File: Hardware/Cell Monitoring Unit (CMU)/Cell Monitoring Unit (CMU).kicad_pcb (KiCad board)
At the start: 4 copper layers, 144.7 x 95.9 mm, 171 parts, among them J1 TEST, J10 NTC-5, J11 NTC-6, J12 NTC-7, J13 NTC-8, J2 LOW SIDE, J3 12S, J4 705550056, J5 HIGH SIDE, J6 NTC-1, J7 NTC-2, J8 NTC-3, J9 NTC-4, T1 CEP99-102, T2 CEP99-102, U1 PESD5V0L2BT, U2 PESD5V0L2BT, U3 ZXTN4004KQTC, U4 PBQ79616PAPTQ1

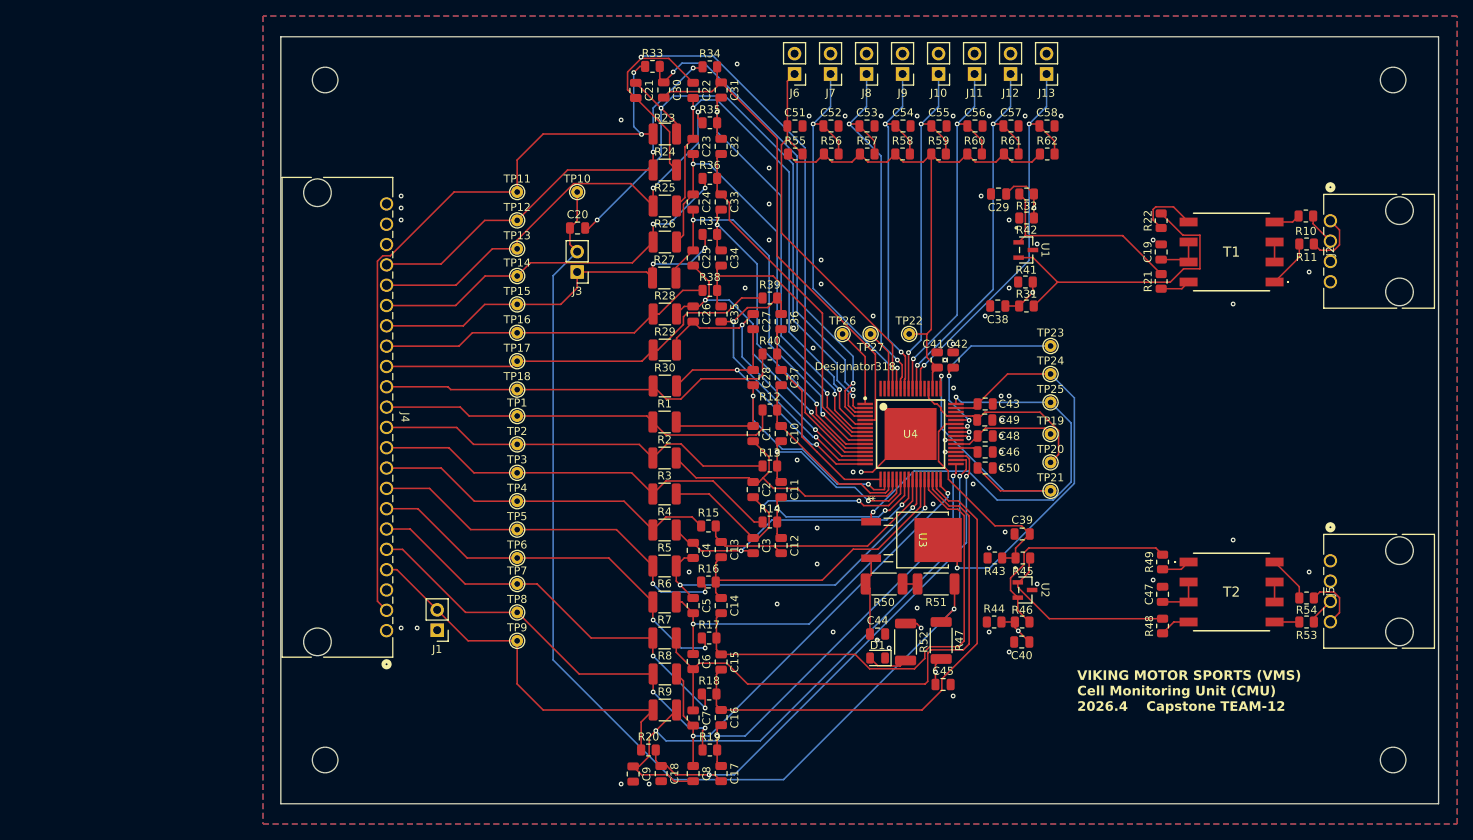
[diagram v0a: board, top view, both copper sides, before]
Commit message: Big schematic cleanup - made into hierarchical schematic, lots of checking on power, more text notes.
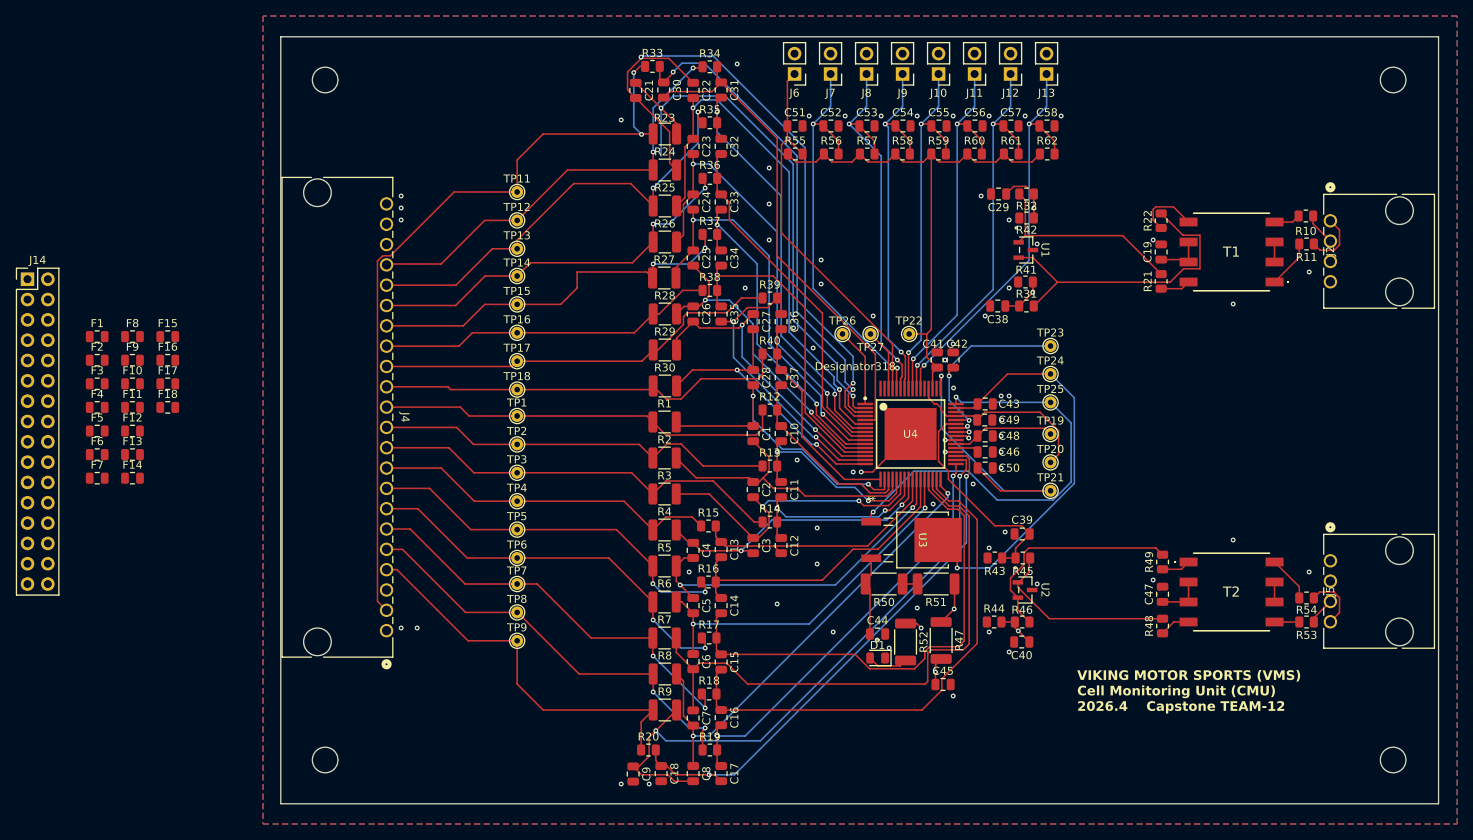
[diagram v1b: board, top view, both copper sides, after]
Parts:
- removed C20: 0.47uF, Capacitor_SMD:C_0805_2012Metric
- removed J1: TEST, Connector_PinHeader_2.54mm:PinHeader_1x02_P2.54mm_Vertical
- removed J3: 12S, Connector_PinHeader_2.54mm:PinHeader_1x02_P2.54mm_Vertical
- removed TP10: TestPoint_Square, TestPoint:TestPoint_THTPad_D1.5mm_Drill0.7mm
- added F1: 1A, Fuse:Fuse_0805_2012Metric, F.Cu at (48.0, 88.6)
- added F10: 1A, Fuse:Fuse_0805_2012Metric, F.Cu at (52.4, 94.5)
- added F11: 1A, Fuse:Fuse_0805_2012Metric, F.Cu at (52.4, 97.4)
- added F12: 1A, Fuse:Fuse_0805_2012Metric, F.Cu at (52.4, 100.4)
- added F13: 1A, Fuse:Fuse_0805_2012Metric, F.Cu at (52.4, 103.3)
- added F14: 1A, Fuse:Fuse_0805_2012Metric, F.Cu at (52.4, 106.3)
- added F15: 1A, Fuse:Fuse_0805_2012Metric, F.Cu at (56.8, 88.6)
- added F16: 1A, Fuse:Fuse_0805_2012Metric, F.Cu at (56.8, 91.5)
- added F17: 1A, Fuse:Fuse_0805_2012Metric, F.Cu at (56.8, 94.5)
- added F18: 1A, Fuse:Fuse_0805_2012Metric, F.Cu at (56.8, 97.4)
- added F2: 1A, Fuse:Fuse_0805_2012Metric, F.Cu at (48.0, 91.5)
- added F3: 1A, Fuse:Fuse_0805_2012Metric, F.Cu at (48.0, 94.5)
- added F4: 1A, Fuse:Fuse_0805_2012Metric, F.Cu at (48.0, 97.4)
- added F5: 1A, Fuse:Fuse_0805_2012Metric, F.Cu at (48.0, 100.4)
- added F6: 1A, Fuse:Fuse_0805_2012Metric, F.Cu at (48.0, 103.3)
- added F7: 1A, Fuse:Fuse_0805_2012Metric, F.Cu at (48.0, 106.3)
- added F8: 1A, Fuse:Fuse_0805_2012Metric, F.Cu at (52.4, 88.6)
- added F9: 1A, Fuse:Fuse_0805_2012Metric, F.Cu at (52.4, 91.5)
- added J14: JUMPER, Connector_PinHeader_2.54mm:PinHeader_2x16_P2.54mm_Vertical, F.Cu at (39.3, 81.4)
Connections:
- net /COMHN_OPT renamed /Transformer Isolation/COMHN_OPT
- net /COMHP_OPT renamed /Transformer Isolation/COMHP_OPT
- net /COMLN_OPT renamed /Transformer Isolation/COMLN_OPT
- net /COMLP_OPT renamed /Transformer Isolation/COMLP_OPT
- net /GPIO1 renamed /BQ79616/GPIO1
- net /GPIO2 renamed /BQ79616/GPIO2
- net /GPIO3 renamed /BQ79616/GPIO3
- net /GPIO4 renamed /BQ79616/GPIO4
- net /GPIO5 renamed /BQ79616/GPIO5
- net /GPIO6 renamed /BQ79616/GPIO6
- net /GPIO7 renamed /BQ79616/GPIO7
- net /GPIO8 renamed /BQ79616/GPIO8
- net /ISO COMHN renamed /Transformer Isolation/ISO_COMHN
- net /ISO COMHP renamed /Transformer Isolation/ISO_COMHP
- net /ISO COMLN renamed /Transformer Isolation/ISO_COMLN
- net /ISO COMLP renamed /Transformer Isolation/ISO_COMLP
- net /LDOIN renamed /BQ79616/LDOIN
- net /NPNB renamed /BQ79616/NPNB
- net /TSREF renamed /BQ79616/TSREF
- net BAT_TOP renamed /BQ79616/PWR
- net CB0 renamed /BQ79616/CB0
- net CB1 renamed /BQ79616/CB1
- net CB10 renamed /BQ79616/CB10
- net CB11 renamed /BQ79616/CB11
- net CB12 renamed /BQ79616/CB12
- net CB13 renamed /BQ79616/CB13
- net CB14 renamed /BQ79616/CB14
- net CB15 renamed /BQ79616/CB15
- net CB16 renamed /BQ79616/CB16
- net CB2 renamed /BQ79616/CB2
- net CB3 renamed /BQ79616/CB3
- net CB4 renamed /BQ79616/CB4
- net CB5 renamed /BQ79616/CB5
- net CB6 renamed /BQ79616/CB6
- net CB7 renamed /BQ79616/CB7
- net CB8 renamed /BQ79616/CB8
- net CB9 renamed /BQ79616/CB9
- net COMHN renamed /BQ79616/COMHN
- net COMHP renamed /BQ79616/COMHP
- net COMLN renamed /BQ79616/COMLN
- net COMLP renamed /BQ79616/COMLP
- net VC0 renamed /BQ79616/VC0
- net VC1 renamed /BQ79616/VC1
- net VC10 renamed /BQ79616/VC10
- net VC11 renamed /BQ79616/VC11
- net VC12 renamed /BQ79616/VC12
- net VC13 renamed /BQ79616/VC13
- net VC14 renamed /BQ79616/VC14
- net VC15 renamed /BQ79616/VC15
- net VC16 renamed /BQ79616/VC16
- net VC2 renamed /BQ79616/VC2
- net VC3 renamed /BQ79616/VC3
- net VC4 renamed /BQ79616/VC4
- net VC5 renamed /BQ79616/VC5
- net VC6 renamed /BQ79616/VC6
- net VC7 renamed /BQ79616/VC7
- net VC8 renamed /BQ79616/VC8
- net VC9 renamed /BQ79616/VC9
- J4 pad 10: CELL6 -> /CELL6
- J4 pad 11: CELL7 -> /CELL7
- J4 pad 12: CELL8 -> /CELL8
- J4 pad 13: CELL9 -> /CELL9
- J4 pad 14: CELL10 -> /CELL10
- J4 pad 15: CELL11 -> /CELL11
- J4 pad 16: CELL12 -> /CELL12
- J4 pad 17: CELL13 -> /CELL13
- J4 pad 18: CELL14 -> /CELL14
- J4 pad 19: CELL15 -> /CELL15
- J4 pad 2: CELL16 -> /CELL16-UNP
- J4 pad 21: CELL0 -> /CELL16-UNP
- J4 pad 5: CELL1 -> /CELL1-UNP
- J4 pad 6: CELL2 -> /CELL2-UNP
- J4 pad 7: CELL3 -> /CELL3-UNP
- J4 pad 8: CELL4 -> /CELL4
- J4 pad 9: CELL5 -> /CELL5
- R1 pad 1: CELL8 -> /Cell filtering and balancing/CELL8
- R12 pad 1: CELL8 -> /Cell filtering and balancing/CELL8
- R13 pad 1: CELL7 -> /Cell filtering and balancing/CELL7
- R14 pad 1: CELL6 -> /Cell filtering and balancing/CELL6
- R15 pad 1: CELL5 -> /Cell filtering and balancing/CELL5
- R16 pad 1: CELL4 -> /Cell filtering and balancing/CELL4
- R17 pad 1: CELL3 -> /Cell filtering and balancing/CELL3
- R18 pad 1: CELL2 -> /Cell filtering and balancing/CELL2
- R19 pad 1: CELL1 -> /Cell filtering and balancing/CELL1
- R2 pad 1: CELL7 -> /Cell filtering and balancing/CELL7
- R23 pad 1: CELL16 -> /Cell filtering and balancing/CELL16S
- R24 pad 1: CELL15 -> /Cell filtering and balancing/CELL15
- R25 pad 1: CELL14 -> /Cell filtering and balancing/CELL14
- R26 pad 1: CELL13 -> /Cell filtering and balancing/CELL13
- R27 pad 1: CELL12 -> /Cell filtering and balancing/CELL12
- R28 pad 1: CELL11 -> /Cell filtering and balancing/CELL11
- R29 pad 1: CELL10 -> /Cell filtering and balancing/CELL10
- R3 pad 1: CELL6 -> /Cell filtering and balancing/CELL6
- R30 pad 1: CELL9 -> /Cell filtering and balancing/CELL9
- R33 pad 1: CELL16 -> /Cell filtering and balancing/CELL16S
- R34 pad 1: CELL15 -> /Cell filtering and balancing/CELL15
- R35 pad 1: CELL14 -> /Cell filtering and balancing/CELL14
- R36 pad 1: CELL13 -> /Cell filtering and balancing/CELL13
- R37 pad 1: CELL12 -> /Cell filtering and balancing/CELL12
- R38 pad 1: CELL11 -> /Cell filtering and balancing/CELL11
- R39 pad 1: CELL10 -> /Cell filtering and balancing/CELL10
- R4 pad 1: CELL5 -> /Cell filtering and balancing/CELL5
- R40 pad 1: CELL9 -> /Cell filtering and balancing/CELL9
- R5 pad 1: CELL4 -> /Cell filtering and balancing/CELL4
- R6 pad 1: CELL3 -> /Cell filtering and balancing/CELL3
- R7 pad 1: CELL2 -> /Cell filtering and balancing/CELL2
- R8 pad 1: CELL1 -> /Cell filtering and balancing/CELL1
- TP1 pad 1: CELL8 -> /Cell filtering and balancing/CELL8
- TP11 pad 1: CELL16 -> /Cell filtering and balancing/CELL16S
- TP12 pad 1: CELL15 -> /Cell filtering and balancing/CELL15
- TP13 pad 1: CELL14 -> /Cell filtering and balancing/CELL14
- TP14 pad 1: CELL13 -> /Cell filtering and balancing/CELL13
- TP15 pad 1: CELL12 -> /Cell filtering and balancing/CELL12
- TP16 pad 1: CELL11 -> /Cell filtering and balancing/CELL11
- TP17 pad 1: CELL10 -> /Cell filtering and balancing/CELL10
- TP18 pad 1: CELL9 -> /Cell filtering and balancing/CELL9
- TP2 pad 1: CELL7 -> /Cell filtering and balancing/CELL7
- TP3 pad 1: CELL6 -> /Cell filtering and balancing/CELL6
- TP4 pad 1: CELL5 -> /Cell filtering and balancing/CELL5
- TP5 pad 1: CELL4 -> /Cell filtering and balancing/CELL4
- TP6 pad 1: CELL3 -> /Cell filtering and balancing/CELL3
- TP7 pad 1: CELL2 -> /Cell filtering and balancing/CELL2
- TP8 pad 1: CELL1 -> /Cell filtering and balancing/CELL1
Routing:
- net (no net): track 0.00 -> 850.9 mm, vias 0 -> 18
- net /BQ79616/PWR: track 131.1 -> 5.44 mm
- net CELL16: track 97.4 -> 0.00 mm, vias 2 -> 0
- net CELL14: track 56.1 -> 0.00 mm, vias 2 -> 0
- net CELL15: track 54.3 -> 0.00 mm, vias 2 -> 0
- net CELL1: track 53.3 -> 0.00 mm, vias 2 -> 0
- net CELL2: track 52.3 -> 0.00 mm, vias 2 -> 0
- net CELL6: track 52.2 -> 0.00 mm
- net CELL9: track 51.8 -> 0.00 mm
- net CELL10: track 51.1 -> 0.00 mm
- net CELL8: track 51.1 -> 0.00 mm
- net CELL7: track 50.4 -> 0.00 mm
- net CELL3: track 49.8 -> 0.00 mm, vias 2 -> 0
- net CELL13: track 48.6 -> 0.00 mm, vias 2 -> 0
- net CELL12: track 48.5 -> 0.00 mm, vias 2 -> 0
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
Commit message: Add keepout rules for high voltage areas
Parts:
- moved F18 38.7 mm to (88.0, 74.5), turned to 180 degrees
- moved TP23 9.25 mm to (167.2, 99.0)
- moved TP20 9.20 mm to (167.2, 95.1)
- moved C42 8.50 mm to (159.0, 99.0), turned to 0 degrees
- moved R54 5.05 mm to (199.2, 126.3)
- moved C43 2.10 mm to (159.0, 94.9)
- moved C49 2.10 mm to (158.9, 96.9)
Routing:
- net Net-(U4-NEG5V): track 24.3 -> 12.8 mm, vias 2 -> 0
- net Net-(R54-Pad2): track 5.78 -> 15.6 mm
- net Net-(U4-CVDD): track 63.1 -> 53.3 mm
- net /Transformer Isolation/ISO_COMHN: track 7.29 -> 3.59 mm
- net /CELL16-UNP: track 0.00 -> 2.90 mm
- net /BQ79616/LDOIN: track 52.0 -> 53.8 mm
- net /BQ79616/NPNB: track 54.6 -> 55.6 mm
- net /Transformer Isolation/ISO_COMHP: track 3.43 -> 4.03 mm
- net CELL0: vias 67 -> 62

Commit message: updated cmu layout
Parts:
- removed the C49 at (158.9, 96.9)
- added C40: 4.7u, Capacitor_SMD:C_0805_2012Metric, F.Cu at (159.0, 98.0)
- D1: value LED -> GRN
- moved J2 68.2 mm to (107.5, 81.7)
- moved F1 52.4 mm to (88.0, 122.5), turned to 180 degrees
- moved F2 46.6 mm to (88.0, 115.5), turned to 180 degrees
- moved F3 44.1 mm to (88.0, 113.0), turned to 180 degrees
- moved F4 42.1 mm to (88.0, 110.5), turned to 180 degrees
- moved F14 41.7 mm to (88.0, 84.5), turned to 180 degrees
- moved F5 40.7 mm to (88.0, 108.0), turned to 180 degrees
- moved F7 40.1 mm to (88.0, 103.0), turned to 180 degrees
- moved F6 40.1 mm to (88.0, 105.5), turned to 180 degrees
- moved F13 39.2 mm to (88.0, 87.0), turned to 180 degrees
- moved F8 37.5 mm to (88.0, 100.5), turned to 180 degrees
- moved F12 37.1 mm to (87.9, 89.5), turned to 180 degrees
- moved F9 36.0 mm to (88.0, 97.0), turned to 180 degrees
- moved F11 36.0 mm to (88.0, 92.0), turned to 180 degrees
- moved F18 35.7 mm to (88.0, 77.0), turned to 180 degrees
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- renumbered C21 to C19, C22 to C20, C23 to C21, C24 to C22, C25 to C23, C26 to C24, C27 to C25, C28 to C26, C30 to C27, C31 to C28, C32 to C29, C33 to C30, C34 to C31, C35 to C32, C36 to C33, C37 to C34, C43 to C35, C44 to C36, C45 to C37, C46 to C38, C48 to C39, C42 to C41, C50 to C42, C41 to C43, C51 to C44, C52 to C45, C53 to C46, C54 to C47, C55 to C48, C56 to C49, C57 to C50, C58 to C51, C38 to C52, C39 to C53, C29 to C54, C40 to C55, C47 to C56, C19 to C57, F18 to F17, F17 to F18, J4 to J1, J11 to J10, J12 to J11, J13 to J12, J14 to J2, J5 to J3, J2 to J4, J6 to J5, J7 to J6, J8 to J7, J9 to J8, J10 to J9, R12 to R10, R13 to R11, R14 to R12, R15 to R13, R16 to R14, R17 to R15, R18 to R16, R19 to R17, R20 to R18, R23 to R19, R24 to R20, R25 to R21, R26 to R22, R27 to R23, R28 to R24, R29 to R25, R30 to R26, R33 to R27, R34 to R28, R35 to R29, R36 to R30, R37 to R31, R38 to R32, R39 to R33, R40 to R34, R50 to R35, R51 to R36, R47 to R37, R52 to R38, R55 to R39, R56 to R40, R57 to R41, R58 to R42, R59 to R43, R60 to R44, R61 to R45, R62 to R46, R41 to R47, R42 to R48, R43 to R49, R44 to R50, R31 to R51, R32 to R52, R45 to R53, R46 to R54, R48 to R55, R49 to R56, R22 to R57, R21 to R58, R10 to R59, R11 to R60, R53 to R61, R54 to R62, T2 to T1, T1 to T2, TP11 to TP10, TP12 to TP11, TP13 to TP12, TP14 to TP13, TP15 to TP14, TP16 to TP15, TP17 to TP16, TP18 to TP17, TP19 to TP18, TP20 to TP19, TP21 to TP20, TP23 to TP21, TP24 to TP22, TP25 to TP23, TP26 to TP24, TP27 to TP25, TP22 to TP26, U3 to U1, U4 to U2, U1 to U3, U2 to U4
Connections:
- net /BQ79616/CB0 renamed /CMU-BQ79616 AFE Core/CB0
- net /BQ79616/CB1 renamed /CMU-BQ79616 AFE Core/CB1
- net /BQ79616/CB10 renamed /CMU-BQ79616 AFE Core/CB10
- net /BQ79616/CB11 renamed /CMU-BQ79616 AFE Core/CB11
- net /BQ79616/CB12 renamed /CMU-BQ79616 AFE Core/CB12
- net /BQ79616/CB13 renamed /CMU-BQ79616 AFE Core/CB13
- net /BQ79616/CB14 renamed /CMU-BQ79616 AFE Core/CB14
- net /BQ79616/CB15 renamed /CMU-BQ79616 AFE Core/CB15
- net /BQ79616/CB16 renamed /CMU-BQ79616 AFE Core/CB16
- net /BQ79616/CB2 renamed /CMU-BQ79616 AFE Core/CB2
- net /BQ79616/CB3 renamed /CMU-BQ79616 AFE Core/CB3
- net /BQ79616/CB4 renamed /CMU-BQ79616 AFE Core/CB4
- net /BQ79616/CB5 renamed /CMU-BQ79616 AFE Core/CB5
- net /BQ79616/CB6 renamed /CMU-BQ79616 AFE Core/CB6
- net /BQ79616/CB7 renamed /CMU-BQ79616 AFE Core/CB7
- net /BQ79616/CB8 renamed /CMU-BQ79616 AFE Core/CB8
- net /BQ79616/CB9 renamed /CMU-BQ79616 AFE Core/CB9
- net /BQ79616/COMHN renamed /CMU-BQ79616 AFE Core/COMHN
- net /BQ79616/COMHP renamed /CMU-BQ79616 AFE Core/COMHP
- net /BQ79616/COMLN renamed /CMU-BQ79616 AFE Core/COMLN
- net /BQ79616/COMLP renamed /CMU-BQ79616 AFE Core/COMLP
- net /BQ79616/GPIO1 renamed /CMU-BQ79616 AFE Core/GPIO1
- net /BQ79616/GPIO2 renamed /CMU-BQ79616 AFE Core/GPIO2
- net /BQ79616/GPIO3 renamed /CMU-BQ79616 AFE Core/GPIO3
- net /BQ79616/GPIO4 renamed /CMU-BQ79616 AFE Core/GPIO4
- net /BQ79616/GPIO5 renamed /CMU-BQ79616 AFE Core/GPIO5
- net /BQ79616/GPIO6 renamed /CMU-BQ79616 AFE Core/GPIO6
- net /BQ79616/GPIO7 renamed /CMU-BQ79616 AFE Core/GPIO7
- net /BQ79616/GPIO8 renamed /CMU-BQ79616 AFE Core/GPIO8
- net /BQ79616/LDOIN renamed /CMU-BQ79616 AFE Core/LDOIN
- net /BQ79616/NPNB renamed /CMU-BQ79616 AFE Core/NPNB
- net /BQ79616/PWR renamed /CMU-BQ79616 AFE Core/PWR
- net /BQ79616/TSREF renamed /CMU-BQ79616 AFE Core/TSREF
- net /BQ79616/VC0 renamed /CMU-BQ79616 AFE Core/VC0
- net /BQ79616/VC1 renamed /CMU-BQ79616 AFE Core/VC1
- net /BQ79616/VC10 renamed /CMU-BQ79616 AFE Core/VC10
- net /BQ79616/VC11 renamed /CMU-BQ79616 AFE Core/VC11
- net /BQ79616/VC12 renamed /CMU-BQ79616 AFE Core/VC12
- net /BQ79616/VC13 renamed /CMU-BQ79616 AFE Core/VC13
- net /BQ79616/VC14 renamed /CMU-BQ79616 AFE Core/VC14
- net /BQ79616/VC15 renamed /CMU-BQ79616 AFE Core/VC15
- net /BQ79616/VC16 renamed /CMU-BQ79616 AFE Core/VC16
- net /BQ79616/VC2 renamed /CMU-BQ79616 AFE Core/VC2
- net /BQ79616/VC3 renamed /CMU-BQ79616 AFE Core/VC3
- net /BQ79616/VC4 renamed /CMU-BQ79616 AFE Core/VC4
- net /BQ79616/VC5 renamed /CMU-BQ79616 AFE Core/VC5
- net /BQ79616/VC6 renamed /CMU-BQ79616 AFE Core/VC6
- net /BQ79616/VC7 renamed /CMU-BQ79616 AFE Core/VC7
- net /BQ79616/VC8 renamed /CMU-BQ79616 AFE Core/VC8
- net /BQ79616/VC9 renamed /CMU-BQ79616 AFE Core/VC9
- net /Cell filtering and balancing/CELL1 renamed /CMU-Cell Filtering & Balancing/CELL1
- net /Cell filtering and balancing/CELL10 renamed /CMU-Cell Filtering & Balancing/CELL10
- net /Cell filtering and balancing/CELL11 renamed /CMU-Cell Filtering & Balancing/CELL11
- net /Cell filtering and balancing/CELL12 renamed /CMU-Cell Filtering & Balancing/CELL12
- net /Cell filtering and balancing/CELL13 renamed /CMU-Cell Filtering & Balancing/CELL13
- net /Cell filtering and balancing/CELL14 renamed /CMU-Cell Filtering & Balancing/CELL14
- net /Cell filtering and balancing/CELL15 renamed /CMU-Cell Filtering & Balancing/CELL15
- net /Cell filtering and balancing/CELL16S renamed /CMU-Cell Filtering & Balancing/CELL16S
- net /Cell filtering and balancing/CELL2 renamed /CMU-Cell Filtering & Balancing/CELL2
- net /Cell filtering and balancing/CELL3 renamed /CMU-Cell Filtering & Balancing/CELL3
- net /Cell filtering and balancing/CELL4 renamed /CMU-Cell Filtering & Balancing/CELL4
- net /Cell filtering and balancing/CELL5 renamed /CMU-Cell Filtering & Balancing/CELL5
- net /Cell filtering and balancing/CELL6 renamed /CMU-Cell Filtering & Balancing/CELL6
- net /Cell filtering and balancing/CELL7 renamed /CMU-Cell Filtering & Balancing/CELL7
- net /Cell filtering and balancing/CELL8 renamed /CMU-Cell Filtering & Balancing/CELL8
- net /Cell filtering and balancing/CELL9 renamed /CMU-Cell Filtering & Balancing/CELL9
- net /Transformer Isolation/COMHN_OPT renamed /CMU-Daisy-Chain Interface/COMHN_OPT
- net /Transformer Isolation/COMHP_OPT renamed /CMU-Daisy-Chain Interface/COMHP_OPT
- net /Transformer Isolation/COMLN_OPT renamed /CMU-Daisy-Chain Interface/COMLN_OPT
- net /Transformer Isolation/COMLP_OPT renamed /CMU-Daisy-Chain Interface/COMLP_OPT
- net /Transformer Isolation/ISO_COMHN renamed /CMU-Daisy-Chain Interface/ISO_COMHN
- net /Transformer Isolation/ISO_COMHP renamed /CMU-Daisy-Chain Interface/ISO_COMHP
- net /Transformer Isolation/ISO_COMLN renamed /CMU-Daisy-Chain Interface/ISO_COMLN
- net /Transformer Isolation/ISO_COMLP renamed /CMU-Daisy-Chain Interface/ISO_COMLP
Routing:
- net (no net): track 850.9 -> 0.00 mm, vias 18 -> 0
- net /CMU-Cell Filtering & Balancing/CELL15: track 0.00 -> 141.4 mm, vias 0 -> 2
- net /CMU-Cell Filtering & Balancing/CELL1: track 0.00 -> 111.8 mm, vias 0 -> 2
- net /CMU-Cell Filtering & Balancing/CELL2: track 0.00 -> 105.4 mm, vias 0 -> 2
- net Net-(J2-Pin_16): track 0.00 -> 97.3 mm, vias 0 -> 2
- net /CMU-Cell Filtering & Balancing/CELL14: track 0.00 -> 91.3 mm, vias 0 -> 2
- net /CMU-Cell Filtering & Balancing/CELL3: track 0.00 -> 90.7 mm, vias 0 -> 2
- net /CMU-Cell Filtering & Balancing/CELL4: track 0.00 -> 85.0 mm, vias 0 -> 2
- net /CMU-Cell Filtering & Balancing/CELL6: track 0.00 -> 77.3 mm
- net /CMU-BQ79616 AFE Core/PWR: track 5.44 -> 80.3 mm
- net /CMU-Cell Filtering & Balancing/CELL5: track 0.00 -> 73.3 mm
- net /CMU-Cell Filtering & Balancing/CELL13: track 0.00 -> 72.1 mm, vias 0 -> 2
- net /CMU-Cell Filtering & Balancing/CELL7: track 0.00 -> 64.0 mm
- net /CMU-Cell Filtering & Balancing/CELL8: track 0.00 -> 62.5 mm
- net /CMU-Cell Filtering & Balancing/CELL12: track 0.00 -> 59.8 mm, vias 0 -> 2
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- added copper zone on B.Cu, net /CMU-BQ79616 AFE Core/PWR
- added copper zone on F.Cu, net /CMU-BQ79616 AFE Core/PWR
- added copper zone on In1.Cu, net /CMU-BQ79616 AFE Core/PWR
- added copper zone on In2.Cu, net /CMU-BQ79616 AFE Core/PWR
